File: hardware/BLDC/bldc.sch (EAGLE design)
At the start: 83 parts, among them J1 PWR_2_XT30PW-M, J2 LINEAR_3_JST_PH_RA, J3 LINEAR_8_JST_PH_RA, U1 MA702, U10 MCP2542FD, U11 LDFM33PUR, U2 DRV8323RS, U3 TPN7R006PL, U4 TPN7R006PL, U5 TPN7R006PL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

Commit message: Prior to enlarging 24v plane
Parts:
- C1, C34, C35: value 1uf 10v -> 1uF 10V
- C13, C15, C2, C36, C4, C41, C43, C6, C7, C8: value 100nF 10V -> 0.1uF 10V
- C14: value 10uF 50V -> 10uF 25V
- C31, C32: value 1uf 50v -> 1uF 50V
- C33: value 47nF 50v -> 47nF 50V
- C37, C42: value 6.8pF 10V -> 10pF 10V
- J2: value LINEAR_3_JST_PH_RA -> LINEAR_35040500391; device _T_conn:LINEAR_3_JST_PH_RA -> _T_conn:LINEAR_35040500391
- J3: value LINEAR_8_JST_PH_RA -> LINEAR_85040500891; device _T_conn:LINEAR_8_JST_PH_RA -> _T_conn:LINEAR_85040500891
- R8, R9: value 10k -> 10k 1%
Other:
- moved on the sheet: J2, J3

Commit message: OCD kicking in for traces :)
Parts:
- D1: value SCHOTTKY_SOD123 -> (none)
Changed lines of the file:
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@@
 <part name="PHASE_B" library="_T_conn" library_urn="urn:adsk.eagle:library:19570503" deviceset="WIRE_HOLE" device="_AWG_18" package3d_urn="urn:adsk.eagle:package:20293989/2"/>
 <part name="PHASE_C" library="_T_conn" library_urn="urn:adsk.eagle:library:19570503" deviceset="WIRE_HOLE" device="_AWG_18" package3d_urn="urn:adsk.eagle:package:20293989/2"/>
-<part name="C12" library="_T_rcl" library_urn="urn:adsk.eagle:library:19571919" deviceset="C" device="0603" package3d_urn="urn:adsk.eagle:package:19572011/3" value="2.2uF 50V"/>
+<part name="C12" library="_T_rcl" library_urn="urn:adsk.eagle:library:19571919" deviceset="C" device="0603" package3d_urn="urn:adsk.eagle:package:19572011/4" value="2.2uF 50V"/>
 <part name="R1" library="_T_rcl" library_urn="urn:adsk.eagle:library:19571919" deviceset="R" device="0402" package3d_urn="urn:adsk.eagle:package:19572014/3" value="100k"/>
 <part name="GND9" library="_T_power" library_urn="urn:adsk.eagle:library:19572085" deviceset="GND" device=""/>
 <part name="GND10" library="_T_power" library_urn="urn:adsk.eagle:library:19572085" deviceset="GND" device=""/>
 <part name="C13" library="_T_rcl" library_urn="urn:adsk.eagle:library:19571919" deviceset="C" device="0402" package3d_urn="urn:adsk.eagle:package:19572013/4" value="0.1uF 10V"/>
-<part name="L2" library="_T_rcl" library_urn="urn:adsk.eagle:library:19571919" deviceset="L" device="_SDR0302" package3d_urn="urn:adsk.eagle:package:20294118/5" value="22uH Bourns"/>
+<part name="L2" library="_T_rcl" library_urn="urn:adsk.eagle:library:19571919" deviceset="L" device="_SDR0302" package3d_urn="urn:adsk.eagle:package:20294118/6" value="22uH Bourns"/>
 <part name="R2" library="_T_rcl" library_urn="urn:adsk.eagle:library:19571919" deviceset="R" device="0402" package3d_urn="urn:adsk.eagle:package:19572014/3" value="54.9k 1%"/>
 <part name="R3" library="_T_rcl" library_urn="urn:adsk.eagle:library:19571919" deviceset="R" device="0402" package3d_urn="urn:adsk.eagle:package:19572014/3" value="10k 1%"/>
 <part name="GND11" library="_T_power" library_urn="urn:adsk.eagle:library:19572085" deviceset="GND" device=""/>
-<part name="C14" library="_T_rcl" library_urn="urn:adsk.eagle:library:19571919" deviceset="C" device="0603" package3d_urn="urn:adsk.eagle:package:19572011/3" value="10uF 25V"/>
+<part name="C14" library="_T_rcl" library_urn="urn:adsk.eagle:library:19571919" deviceset="C" device="0603" package3d_urn="urn:adsk.eagle:package:19572011/4" value="10uF 25V"/>
 <part name="GND12" library="_T_power" library_urn="urn:adsk.eagle:library:19572085" deviceset="GND" device=""/>
 <part name="D1" library="_T_rcl" library_urn="urn:adsk.eagle:library:19571919" deviceset="SCHOTTKY" device="_SOD123" package3d_urn="urn:adsk.eagle:package:20295471/2"/>
@@
 <part name="U10" library="_T_ic" library_urn="urn:adsk.eagle:library:19571245" deviceset="MCP2542FD" device="" package3d_urn="urn:adsk.eagle:package:19399098/4"/>
 <part name="R4" library="_T_rcl" library_urn="urn:adsk.eagle:library:19571919" deviceset="R" device="0402" package3d_urn="urn:adsk.eagle:package:19572014/3" value="120"/>
-<part name="C31" library="_T_rcl" library_urn="urn:adsk.eagle:library:19571919" deviceset="C" device="0603" package3d_urn="urn:adsk.eagle:package:19572011/3" value="1uF 50V"/>
+<part name="C31" library="_T_rcl" library_urn="urn:adsk.eagle:library:19571919" deviceset="C" device="0603" package3d_urn="urn:adsk.eagle:package:19572011/4" value="1uF 50V"/>
 <part name="+24V4" library="_T_power" library_urn="urn:adsk.eagle:library:19572085" deviceset="+24V" device=""/>
-<part name="C32" library="_T_rcl" library_urn="urn:adsk.eagle:library:19571919" deviceset="C" device="0603" package3d_urn="urn:adsk.eagle:package:19572011/3" value="1uF 50V"/>
+<part name="C32" library="_T_rcl" library_urn="urn:adsk.eagle:library:19571919" deviceset="C" device="0603" package3d_urn="urn:adsk.eagle:package:19572011/4" value="1uF 50V"/>
 <part name="GND16" library="_T_power" library_urn="urn:adsk.eagle:library:19572085" deviceset="GND" device=""/>
 <part name="GND17" library="_T_power" library_urn="urn:adsk.eagle:library:19572085" deviceset="GND" device=""/>
@@
 <part name="GND18" library="_T_power" library_urn="urn:adsk.eagle:library:19572085" deviceset="GND" device=""/>
 <part name="C35" library="_T_rcl" library_urn="urn:adsk.eagle:library:19571919" deviceset="C" device="0402" package3d_urn="urn:adsk.eagle:package:19572013/4" value="1uF 10V"/>
-<part name="R5" library="_T_rcl" library_urn="urn:adsk.eagle:library:19571919" deviceset="R_SENSE" device="_1210" package3d_urn="urn:adsk.eagle:package:16502583/4" value="0.001"/>
-<part name="R6" library="_T_rcl" library_urn="urn:adsk.eagle:library:19571919" deviceset="R_SENSE" device="_1210" package3d_urn="urn:adsk.eagle:package:16502583/4" value="0.001"/>
-<part name="R7" library="_T_rcl" library_urn="urn:adsk.eagle:library:19571919" deviceset="R_SENSE" device="_1210" package3d_urn="urn:adsk.eagle:package:16502583/4" value="0.001"/>
+<part name="R5" library="_T_rcl" library_urn="urn:adsk.eagle:library:19571919" deviceset="R_SENSE" device="_1210" package3d_urn="urn:adsk.eagle:package:16502583/5" value="0.001"/>
+<part name="R6" library="_T_rcl" library_urn="urn:adsk.eagle:library:19571919" deviceset="R_SENSE" device="_1210" package3d_urn="urn:adsk.eagle:package:16502583/5" value="0.001"/>
+<part name="R7" library="_T_rcl" library_urn="urn:adsk.eagle:library:19571919" deviceset="R_SENSE" device="_1210" package3d_urn="urn:adsk.eagle:package:16502583/5" value="0.001"/>
 <part name="GND19" library="_T_power" library_urn="urn:adsk.eagle:library:19572085" deviceset="GND" device=""/>
 <part name="GND20" library="_T_power" library_urn="urn:adsk.eagle:library:19572085" deviceset="GND" device=""/>
@@
 <part name="+3V3" library="_T_power" library_urn="urn:adsk.eagle:library:19572085" deviceset="+3V3" device=""/>
 <part name="+24V8" library="_T_power" library_urn="urn:adsk.eagle:library:19572085" deviceset="+24V" device=""/>
-<part name="D2" library="_T_rcl" library_urn="urn:adsk.eagle:library:19571919" deviceset="LED" device="_0603" package3d_urn="urn:adsk.eagle:package:19545722/3" value="150060GS75000"/>
-<part name="D3" library="_T_rcl" library_urn="urn:adsk.eagle:library:19571919" deviceset="LED" device="_0603" package3d_urn="urn:adsk.eagle:package:19545722/3" value="150060RS75000"/>
-<part name="D4" library="_T_rcl" library_urn="urn:adsk.eagle:library:19571919" deviceset="LED" device="_0603" package3d_urn="urn:adsk.eagle:package:19545722/3" value="150060BS75000"/>
+<part name="D2" library="_T_rcl" library_urn="urn:adsk.eagle:library:19571919" deviceset="LED" device="_0603" package3d_urn="urn:adsk.eagle:package:19545722/4" value="150060GS75000"/>
+<part name="D3" library="_T_rcl" library_urn="urn:adsk.eagle:library:19571919" deviceset="LED" device="_0603" package3d_urn="urn:adsk.eagle:package:19545722/4" value="150060RS75000"/>
+<part name="D4" library="_T_rcl" library_urn="urn:adsk.eagle:library:19571919" deviceset="LED" device="_0603" package3d_urn="urn:adsk.eagle:package:19545722/4" value="150060BS75000"/>
 <part name="R12" library="_T_rcl" library_urn="urn:adsk.eagle:library:19571919" deviceset="R" device="0402" package3d_urn="urn:adsk.eagle:package:19572014/3" value="22"/>
 <part name="R13" library="_T_rcl" library_urn="urn:adsk.eagle:library:19571919" deviceset="R" device="0402" package3d_urn="urn:adsk.eagle:package:19572014/3" value="270"/>

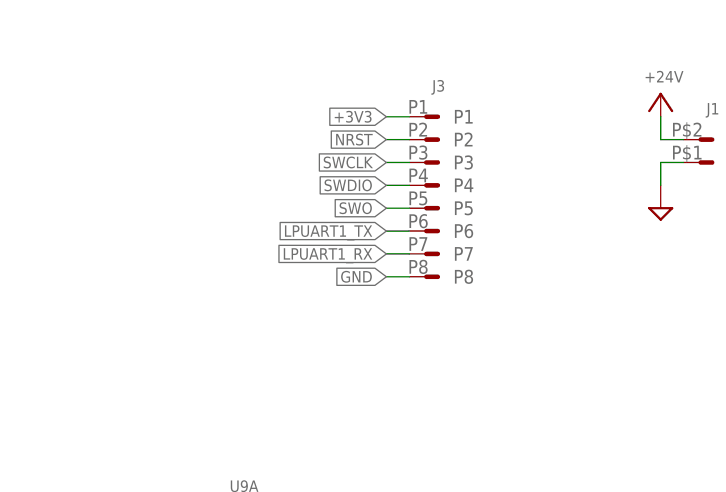
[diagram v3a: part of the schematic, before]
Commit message: Reworked connector and spaced LEDs apart more
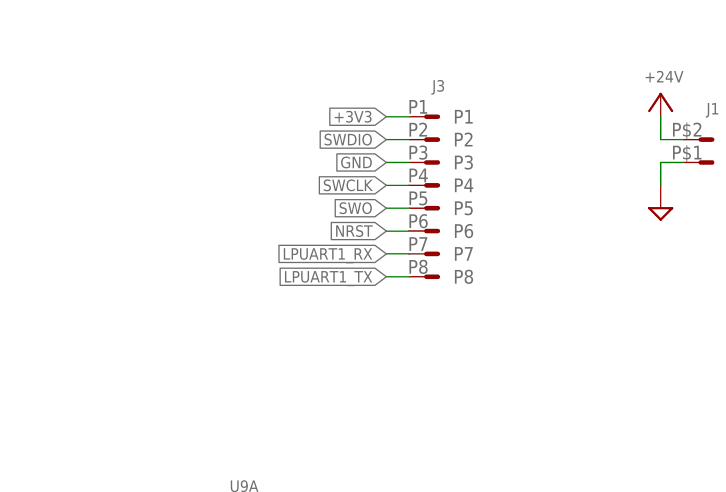
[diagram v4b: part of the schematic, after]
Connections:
- net GND: now also J3.P3; no longer J3.P8
- net LPUART1_TX: now also J3.P8; no longer J3.P6
- net NRST: now also J3.P6; no longer J3.P2
- net SWCLK: now also J3.P4; no longer J3.P3
- net SWDIO: now also J3.P2; no longer J3.P4
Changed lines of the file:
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@@
 </segment>
 <segment>
-<pinref part="J3" gate="G$1" pin="P4"/>
-<wire x1="-35.56" y1="167.64" x2="-38.1" y2="167.64" width="0.1524" layer="91" grouprefs="DEBUG_HEADER"/>
-<label x="-38.1" y="167.64" size="1.27" layer="95" rot="R180" xref="yes" grouprefs="DEBUG_HEADER"/>
+<pinref part="J3" gate="G$1" pin="P2"/>
+<wire x1="-35.56" y1="172.72" x2="-38.1" y2="172.72" width="0.1524" layer="91" grouprefs="DEBUG_HEADER"/>
+<label x="-38.1" y="172.72" size="1.27" layer="95" rot="R180" xref="yes" grouprefs="DEBUG_HEADER"/>
 </segment>
 </net>
@@
 </segment>
 <segment>
-<pinref part="J3" gate="G$1" pin="P3"/>
-<wire x1="-35.56" y1="170.18" x2="-38.1" y2="170.18" width="0.1524" layer="91" grouprefs="DEBUG_HEADER"/>
-<label x="-38.1" y="170.18" size="1.27" layer="95" rot="R180" xref="yes" grouprefs="DEBUG_HEADER"/>
+<pinref part="J3" gate="G$1" pin="P4"/>
+<wire x1="-35.56" y1="167.64" x2="-38.1" y2="167.64" width="0.1524" layer="91" grouprefs="DEBUG_HEADER"/>
+<label x="-38.1" y="167.64" size="1.27" layer="95" rot="R180" xref="yes" grouprefs="DEBUG_HEADER"/>
 </segment>
 </net>
@@
 </segment>
 <segment>
-<pinref part="J3" gate="G$1" pin="P6"/>
-<wire x1="-35.56" y1="162.56" x2="-38.1" y2="162.56" width="0.1524" layer="91" grouprefs="DEBUG_HEADER"/>
-<label x="-38.1" y="162.56" size="1.27" layer="95" rot="R180" xref="yes" grouprefs="DEBUG_HEADER"/>
+<pinref part="J3" gate="G$1" pin="P8"/>
+<wire x1="-35.56" y1="157.48" x2="-38.1" y2="157.48" width="0.1524" layer="91" grouprefs="DEBUG_HEADER"/>
+<label x="-38.1" y="157.48" size="1.27" layer="95" rot="R180" xref="yes" grouprefs="DEBUG_HEADER"/>
 </segment>
 </net>
@@
 </segment>
 <segment>
-<pinref part="J3" gate="G$1" pin="P8"/>
-<wire x1="-35.56" y1="157.48" x2="-38.1" y2="157.48" width="0.1524" layer="91" grouprefs="DEBUG_HEADER"/>
-<label x="-38.1" y="157.48" size="1.27" layer="95" rot="R180" xref="yes" grouprefs="DEBUG_HEADER"/>
-</segment>
-<segment>
 <pinref part="GND5" gate="G$1" pin="GND"/>
 <pinref part="C5" gate="G$1" pin="2"/>
@@
 <pinref part="C43" gate="G$1" pin="2"/>
 <wire x1="17.78" y1="-17.78" x2="17.78" y2="-15.24" width="0.1524" layer="91" grouprefs="UCPOWER"/>
+</segment>
+<segment>
+<pinref part="J3" gate="G$1" pin="P3"/>
+<wire x1="-35.56" y1="170.18" x2="-38.1" y2="170.18" width="0.1524" layer="91" grouprefs="DEBUG_HEADER"/>
+<label x="-38.1" y="170.18" size="1.27" layer="95" rot="R180" xref="yes" grouprefs="DEBUG_HEADER"/>
 </segment>
 </net>
@@
 </segment>
 <segment>
-<pinref part="J3" gate="G$1" pin="P2"/>
-<wire x1="-35.56" y1="172.72" x2="-38.1" y2="172.72" width="0.1524" layer="91" grouprefs="DEBUG_HEADER"/>
-<label x="-38.1" y="172.72" size="1.27" layer="95" rot="R180" xref="yes" grouprefs="DEBUG_HEADER"/>
-</segment>
-</net>
+<pinref part="J3" gate="G$1" pin="P6"/>
+<wire x1="-35.56" y1="162.56" x2="-38.1" y2="162.56" width="0.1524" layer="91" grouprefs="DEBUG_HEADER"/>
+<label x="-38.1" y="162.56" size="1.27" layer="95" rot="R180" xref="yes" grouprefs="DEBUG_HEADER"/>
+</segment>
+</net>

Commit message: Swapped debug pico-lock for PicoBlade
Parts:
- J3: value LINEAR_85040500891 -> LINEAR_8530480810; device _T_conn:LINEAR_85040500891 -> _T_conn:LINEAR_8530480810
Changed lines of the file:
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@@
 <part name="R11" library="_T_rcl" library_urn="urn:adsk.eagle:library:19571919" deviceset="R" device="0402" package3d_urn="urn:adsk.eagle:package:19572014/3" value="10k 1%"/>
 <part name="GND26" library="_T_power" library_urn="urn:adsk.eagle:library:19572085" deviceset="GND" device=""/>
-<part name="J2" library="_T_conn" library_urn="urn:adsk.eagle:library:19570503" deviceset="LINEAR_3" device="5040500391" package3d_urn="urn:adsk.eagle:package:20466869/2" value="LINEAR_35040500391"/>
+<part name="J2" library="_T_conn" library_urn="urn:adsk.eagle:library:19570503" deviceset="LINEAR_3" device="5040500391" package3d_urn="urn:adsk.eagle:package:20466869/3" value="LINEAR_35040500391"/>
 <part name="GND27" library="_T_power" library_urn="urn:adsk.eagle:library:19572085" deviceset="GND" device=""/>
-<part name="J3" library="_T_conn" library_urn="urn:adsk.eagle:library:19570503" deviceset="LINEAR_8" device="5040500891" package3d_urn="urn:adsk.eagle:package:20466410/4" value="LINEAR_85040500891"/>
+<part name="J3" library="_T_conn" library_urn="urn:adsk.eagle:library:19570503" deviceset="LINEAR_8" device="530480810" package3d_urn="urn:adsk.eagle:package:22356850/4" value="LINEAR_8530480810"/>
 <part name="+3V3" library="_T_power" library_urn="urn:adsk.eagle:library:19572085" deviceset="+3V3" device=""/>
 <part name="+24V8" library="_T_power" library_urn="urn:adsk.eagle:library:19572085" deviceset="+24V" device=""/>

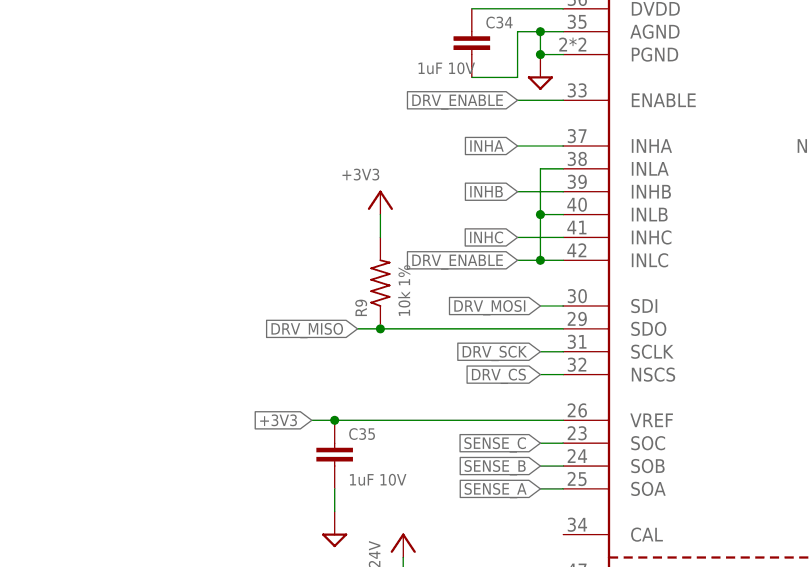
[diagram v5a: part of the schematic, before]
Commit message: Now only using 1k on SDO
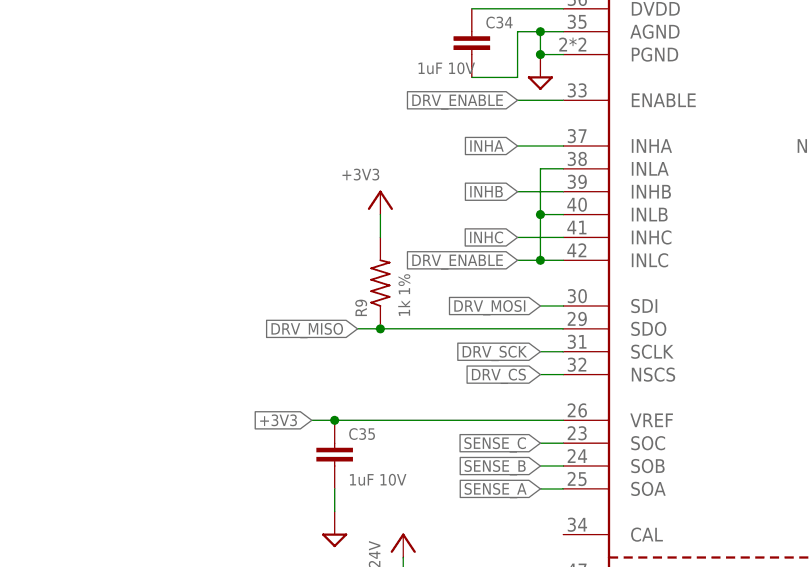
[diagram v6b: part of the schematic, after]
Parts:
- R9: value 10k 1% -> 1k 1%
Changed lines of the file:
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@@
 <part name="R8" library="_T_rcl" library_urn="urn:adsk.eagle:library:19571919" deviceset="R" device="0402" package3d_urn="urn:adsk.eagle:package:19572014/3" value="10k 1%"/>
 <part name="+3V9" library="_T_power" library_urn="urn:adsk.eagle:library:19572085" deviceset="+3V3" device=""/>
-<part name="R9" library="_T_rcl" library_urn="urn:adsk.eagle:library:19571919" deviceset="R" device="0402" package3d_urn="urn:adsk.eagle:package:19572014/3" value="10k 1%"/>
+<part name="R9" library="_T_rcl" library_urn="urn:adsk.eagle:library:19571919" deviceset="R" device="0402" package3d_urn="urn:adsk.eagle:package:19572014/3" value="1k 1%"/>
 <part name="+3V10" library="_T_power" library_urn="urn:adsk.eagle:library:19572085" deviceset="+3V3" device=""/>
 <part name="X1" library="_T_ic" library_urn="urn:adsk.eagle:library:19571245" deviceset="CRYSTAL" device="_NX2016SA-24MHZ-EXS00A-CS11335" package3d_urn="urn:adsk.eagle:package:19324209/4"/>
